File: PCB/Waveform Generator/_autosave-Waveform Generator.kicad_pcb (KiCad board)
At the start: 4 copper layers, 80 x 105.2 mm, 142 parts, among them J1 Power input, J10 USART1_2, J12 Signal 2, J19 ADC_2, J2 RS485_1, J20 TIMER_1, J21 I2C1_1, J22 TIMER_2, J23 I2C1_2, J3 USB_B_Micro, J5 Signal 1, J6 SWD, J7 RS485_2, J8 USART1_1, J9 ADC_1, Q0 AO3401A, Q1 Q_NPN_BCE, Q2 Q_NPN_BCE, Q3 Q_PNP_BCE, Q4 Q_NPN_BCE, Q5 Q_NPN_BCE, Q6 Q_NPN_BCE, Q7 Q_NPN_BCE, Q8 Q_NPN_BCE, SW1 SW_SPDT, SW2 SW_SPDT, SW3 SW_SPDT, U1 STM32F427VITx, U10 USBLC6-2SC6, U11 USBLC6-2SC6, U2 MAX485EESAT, U3 USBLC6-2SC6, U4 OPA1602, U5 OPA1602, U6 USBLC6-2SC6, U7 USBLC6-2SC6, U8 LM335ADT, U9 USBLC6-2SC6, X1 25MHZ

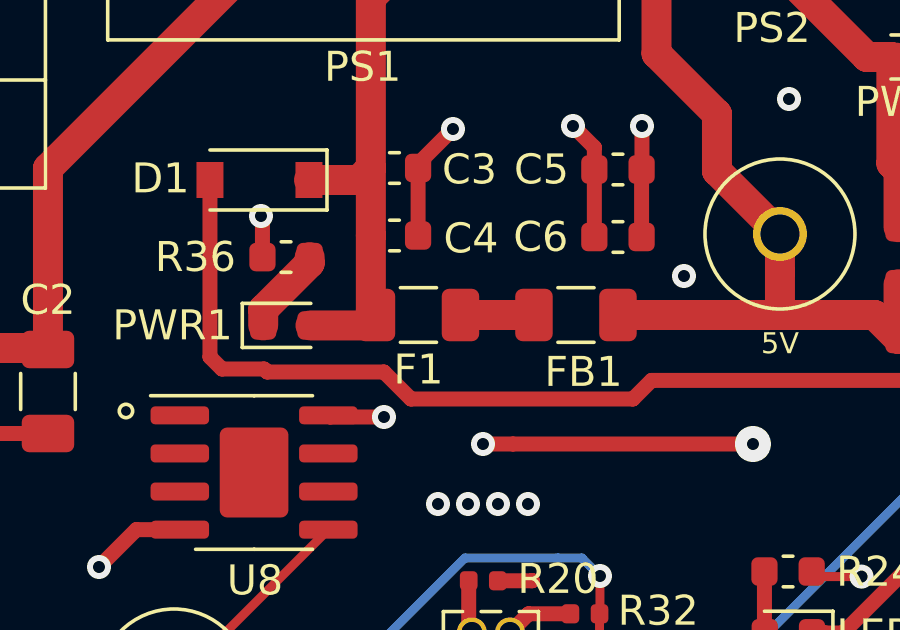
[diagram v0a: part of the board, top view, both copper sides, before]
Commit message: Working on BOM for JLCPCB
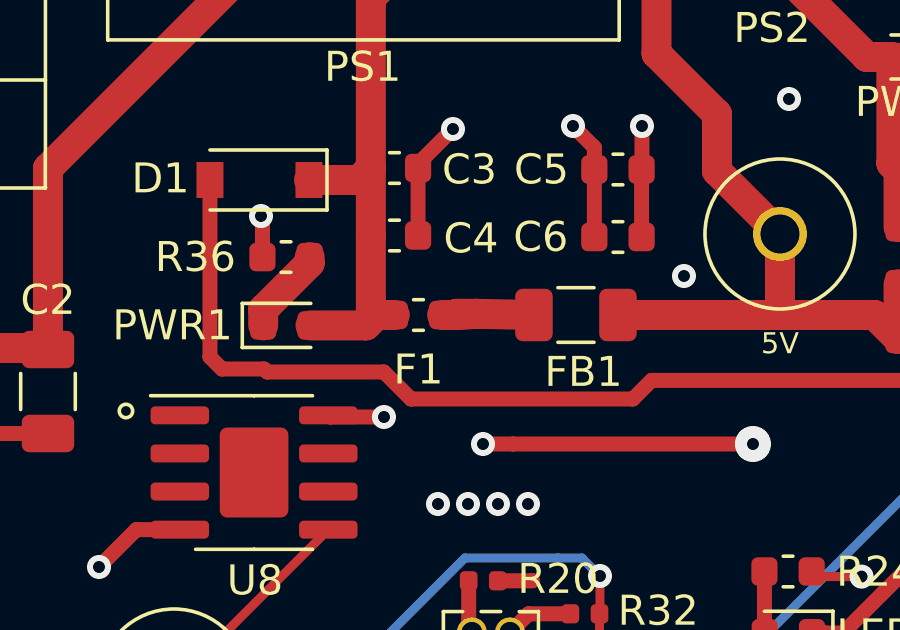
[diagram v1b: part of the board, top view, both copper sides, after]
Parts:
- F1: footprint Fuse:Fuse_1206_3216Metric -> Fuse:Fuse_0603_1608Metric
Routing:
- net Net-(F1-Pad1): track 2.45 -> 4.21 mm
- net Net-(C3-Pad1): track 17.1 -> 17.7 mm
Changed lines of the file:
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@@
     (thickness 1.6)
     (drawings 60)
-    (tracks 1738)
+    (tracks 1744)
     (zones 0)
     (modules 142)
@@
   (layers
     (0 F.Cu signal)
-    (1 In1.Cu power)
-    (2 In2.Cu power)
-    (31 B.Cu signal)
+    (1 In1.Cu power hide)
+    (2 In2.Cu power hide)
+    (31 B.Cu signal hide)
     (32 B.Adhes user)
     (33 F.Adhes user)
@@
   )
   (setup
-    (last_trace_width 0.3)
+    (last_trace_width 1)
     (user_trace_width 0.3)
     (user_trace_width 0.4)
@@
       (drillshape 0)
       (scaleselection 1)
-      (outputdirectory "C:/Users/Nanodyn - Spare/OneDrive - Nanodyn/Desktop/GIT repository/Waveform-generator/PCB/Waveform Generator/gerber/"))
+      (outputdirectory "C:/Users/Nanodyn - Spare/OneDrive - Nanodyn/Desktop/GIT repository/Waveform-generator/PCB/Waveform Generator/assembly/"))
   )
   (net 0 "")
@@
     (add_net VCC)
   )
+  (module Fuse:Fuse_0603_1608Metric (layer F.Cu)
+    (at 56.85 29.7 180)
+    (descr "Fuse SMD 0603 (1608 Metric), square (rectangular) end terminal, IPC_7351 nominal, (Body size source: http://www.tortai-tech.com/upload/download/2011102023233369053.pdf), generated with kicad-footprint-generator")
+    (tags resistor)
+    (attr smd)
+    (fp_text reference F1 (at 0 -1.82) (layer F.SilkS)
+      (effects (font (size 1 1) (thickness 0.15)))
+    )
+    (fp_text value 300mA (at 0 1.82) (layer F.Fab)
+      (effects (font (size 1 1) (thickness 0.15)))
+    )
+    (fp_text user %R (at 0 0) (layer F.Fab)
+      (effects (font (size 0.8 0.8) (thickness 0.12)))
+    )
+    (fp_line (start 1.48 0.73) (end -1.48 0.73) (layer F.CrtYd) (width 0.05))
+    (fp_line (start 1.48 -0.73) (end 1.48 0.73) (layer F.CrtYd) (width 0.05))
+    (fp_line (start -1.48 -0.73) (end 1.48 -0.73) (layer F.CrtYd) (width 0.05))
+    (fp_line (start -1.48 0.73) (end -1.48 -0.73) (layer F.CrtYd) (width 0.05))
+    (fp_line (start -0.162779 0.51) (end 0.162779 0.51) (layer F.SilkS) (width 0.12))
+    (fp_line (start -0.162779 -0.51) (end 0.162779 -0.51) (layer F.SilkS) (width 0.12))
+    (fp_line (start 0.8 0.4) (end -0.8 0.4) (layer F.Fab) (width 0.1))
+    (fp_line (start 0.8 -0.4) (end 0.8 0.4) (layer F.Fab) (width 0.1))
+    (fp_line (start -0.8 -0.4) (end 0.8 -0.4) (layer F.Fab) (width 0.1))
+    (fp_line (start -0.8 0.4) (end -0.8 -0.4) (layer F.Fab) (width 0.1))
+    (pad 2 smd roundrect (at 0.7875 0 180) (size 0.875 0.95) (layers F.Cu F.Paste F.Mask) (roundrect_rratio 0.25)
+      (net 4 "Net-(C3-Pad1)"))
+    (pad 1 smd roundrect (at -0.7875 0 180) (size 0.875 0.95) (layers F.Cu F.Paste F.Mask) (roundrect_rratio 0.25)
+      (net 25 "Net-(F1-Pad1)"))
+    (model ${KISYS3DMOD}/Fuse.3dshapes/Fuse_0603_1608Metric.wrl
+      (at (xyz 0 0 0))
+      (scale (xyz 1 1 1))
+      (rotate (xyz 0 0 0))
+    )
+  )
   (module "Extra Components:5mm Pitch, 2 Way Terminal Block" (layer F.Cu)
     (at 27.15 33.5 270)
@@
   (module LogoSilkScreens:NanodynSilkscreen (layer F.Cu)
     (at 74.35 88)
+    (attr smd)
     (fp_text reference G*** (at 0.9 2.35 180) (layer F.SilkS) hide
       (effects (font (size 1.524 1.524) (thickness 0.3)))
@@
     )
   )
-  (module Fuse:Fuse_1206_3216Metric (layer F.Cu)
-    (at 56.85 29.7 180)
-    (descr "Fuse SMD 1206 (3216 Metric), square (rectangular) end terminal, IPC_7351 nominal, (Body size source: http://www.tortai-tech.com/upload/download/2011102023233369053.pdf), generated with kicad-footprint-generator")
-    (tags resistor)
-    (attr smd)
-    (fp_text reference F1 (at 0 -1.82) (layer F.SilkS)
-      (effects (font (size 1 1) (thickness 0.15)))
-    )
-    (fp_text value 300mA (at 0 1.82) (layer F.Fab)
-      (effects (font (size 1 1) (thickness 0.15)))
-    )
-    (fp_text user %R (at 0 0) (layer F.Fab)
-      (effects (font (size 0.8 0.8) (thickness 0.12)))
-    )
-    (fp_line (start 2.28 1.12) (end -2.28 1.12) (layer F.CrtYd) (width 0.05))
-    (fp_line (start 2.28 -1.12) (end 2.28 1.12) (layer F.CrtYd) (width 0.05))
-    (fp_line (start -2.28 -1.12) (end 2.28 -1.12) (layer F.CrtYd) (width 0.05))
-    (fp_line (start -2.28 1.12) (end -2.28 -1.12) (layer F.CrtYd) (width 0.05))
-    (fp_line (start -0.602064 0.91) (end 0.602064 0.91) (layer F.SilkS) (width 0.12))
-    (fp_line (start -0.602064 -0.91) (end 0.602064 -0.91) (layer F.SilkS) (width 0.12))
-    (fp_line (start 1.6 0.8) (end -1.6 0.8) (layer F.Fab) (width 0.1))
-    (fp_line (start 1.6 -0.8) (end 1.6 0.8) (layer F.Fab) (width 0.1))
-    (fp_line (start -1.6 -0.8) (end 1.6 -0.8) (layer F.Fab) (width 0.1))
-    (fp_line (start -1.6 0.8) (end -1.6 -0.8) (layer F.Fab) (width 0.1))
-    (pad 2 smd roundrect (at 1.4 0 180) (size 1.25 1.75) (layers F.Cu F.Paste F.Mask) (roundrect_rratio 0.2)
-      (net 4 "Net-(C3-Pad1)"))
-    (pad 1 smd roundrect (at -1.4 0 180) (size 1.25 1.75) (layers F.Cu F.Paste F.Mask) (roundrect_rratio 0.2)
-      (net 25 "Net-(F1-Pad1)"))
-    (model ${KISYS3DMOD}/Fuse.3dshapes/Fuse_1206_3216Metric.wrl
-      (at (xyz 0 0 0))
-      (scale (xyz 1 1 1))
-      (rotate (xyz 0 0 0))
-    )
-  )
   (module Inductor_SMD:L_1206_3216Metric (layer F.Cu)
     (at 62.1 29.7)
@@
   (module "Extra Components:TS-1109S-B-B" (layer F.Cu)
     (at 39.243 68.199 90)
+    (attr smd)
     (fp_text reference BTN0 (at 5.199 0 180) (layer F.SilkS)
       (effects (font (size 1 1) (thickness 0.15)))
@@
   (module "Extra Components:TS-1109S-B-B" (layer F.Cu)
     (at 49.5 105.18 270)
+    (attr smd)
     (fp_text reference BTN1 (at -5.23 0.03 180) (layer F.SilkS)
       (effects (font (size 1 1) (thickness 0.15)))
@@
   (module "Extra Components:TS-1109S-B-B" (layer F.Cu)
     (at 40.94 105.2 270)
+    (attr smd)
     (fp_text reference BTN2 (at -5.25 0.05 180) (layer F.SilkS)
       (effects (font (size 1 1) (thickness 0.15)))
@@
   (module "Extra Components:TS-1109S-B-B" (layer F.Cu)
     (at 32.45 105.154 270)
+    (attr smd)
     (fp_text reference BTN3 (at -5.204 0.06 180) (layer F.SilkS)
       (effects (font (size 1 1) (thickness 0.15)))
@@
   (segment (start 55.2625 29.5125) (end 55.45 29.7) (width 1) (layer F.Cu) (net 4) (status 30))
   (segment (start 55.2625 27.05) (end 55.2625 29.5125) (width 1) (layer F.Cu) (net 4) (status 30))
-  (segment (start 55.102 30.048) (end 55.45 29.7) (width 1) (layer F.Cu) (net 4) (status 30))
   (segment (start 53.2495 30.048) (end 55.102 30.048) (width 1) (layer F.Cu) (net 4) (status 30))
   (via (at 64.3 23.4) (size 0.8) (drill 0.4) (layers F.Cu B.Cu) (net 5))
@@
   (segment (start 40.125 90.5375) (end 40.25 90.6625) (width 0.3) (layer F.Cu) (net 24) (status 30))
   (segment (start 38.6 90.5375) (end 40.125 90.5375) (width 0.3) (layer F.Cu) (net 24) (status 30))
-  (segment (start 58.25 29.7) (end 60.7 29.7) (width 1) (layer F.Cu) (net 25) (status 30))
   (segment (start 36.616 29.416) (end 37.8 30.6) (width 1) (layer F.Cu) (net 26) (status 20))
   (segment (start 36.616 20.467) (end 36.616 29.416) (width 1) (layer F.Cu) (net 26) (status 10))
@@
   (via (at 32.6 70.68) (size 0.8) (drill 0.4) (layers F.Cu B.Cu) (net 2) (status 40000))
   (via (at 31.62 72.05) (size 0.8) (drill 0.4) (layers F.Cu B.Cu) (net 2) (status 40000))
+  (segment (start 55.45 29.7) (end 55.102 30.048) (width 1) (layer F.Cu) (net 4))
+  (segment (start 56.0625 29.7) (end 55.45 29.7) (width 1) (layer F.Cu) (net 4))
   (segment (start 69.75 50.75) (end 67.95 50.75) (width 0.3) (layer In2.Cu) (net 9))
   (via (at 69.75 50.75) (size 0.8) (drill 0.4) (layers F.Cu B.Cu) (net 9))
@@
   (segment (start 49.4 72.827) (end 49.39 72.837) (width 0.5) (layer F.Cu) (net 10) (status 30))
   (segment (start 49.4 70.8) (end 49.4 72.827) (width 0.5) (layer F.Cu) (net 10) (status 30))
+  (segment (start 57.6375 29.7) (end 58.25 29.7) (width 0.3) (layer F.Cu) (net 25))
+  (segment (start 58.115 29.66) (end 58.77 29.66) (width 1) (layer F.Cu) (net 25))
+  (segment (start 58.075 29.7) (end 58.115 29.66) (width 1) (layer F.Cu) (net 25))
+  (segment (start 57.6375 29.7) (end 58.075 29.7) (width 1) (layer F.Cu) (net 25))
+  (segment (start 58.25 29.7) (end 58.77 29.66) (width 1) (layer F.Cu) (net 25))
+  (segment (start 58.77 29.66) (end 60.7 29.7) (width 1) (layer F.Cu) (net 25))
   (segment (start 89.3675 22.85) (end 91.0675 22.85) (width 0.3) (layer F.Cu) (net 27) (status 20))
   (segment (start 88.3675 23.85) (end 89.3675 22.85) (width 0.3) (layer F.Cu) (net 27) (status 10))
